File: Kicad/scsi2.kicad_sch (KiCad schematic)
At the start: 30 parts, among them J3 TO-LED, J4 TO-MB, J8 TO-A3000-LED, J9 TO-A3000-MB, U10 NCR53c710 SCSI Host Controller, U13 SST39SF010/020/040, Y1 Abracon ACO-50MHz

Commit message: Add more LCSC parts and mark some parts DNP
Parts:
- C1001, C1003, C1005, C1007, C1009: LCSC Part # (none) -> C14663
- FB1, FB2, FB3, R11: LCSC Part # (none) -> C95177
- J3, J4, J8, J9: LCSC Part # (none) -> C6332196
- R13: LCSC Part # (none) -> C22548
- R9: LCSC Part # (none) -> C114640
- RN10, RN17, RN6, RN7, RN8: LCSC Part # (none) -> C784824
- U13: LCSC Part # (none) -> C72450
- Y1: LCSC Part # (none) -> C7431196

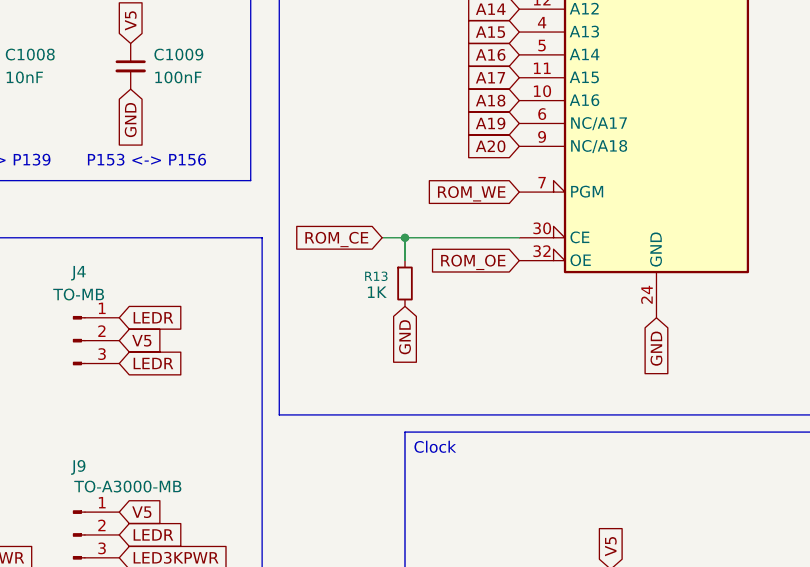
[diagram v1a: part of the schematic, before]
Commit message: Add remaining part numbers, remove C20, C30, C31
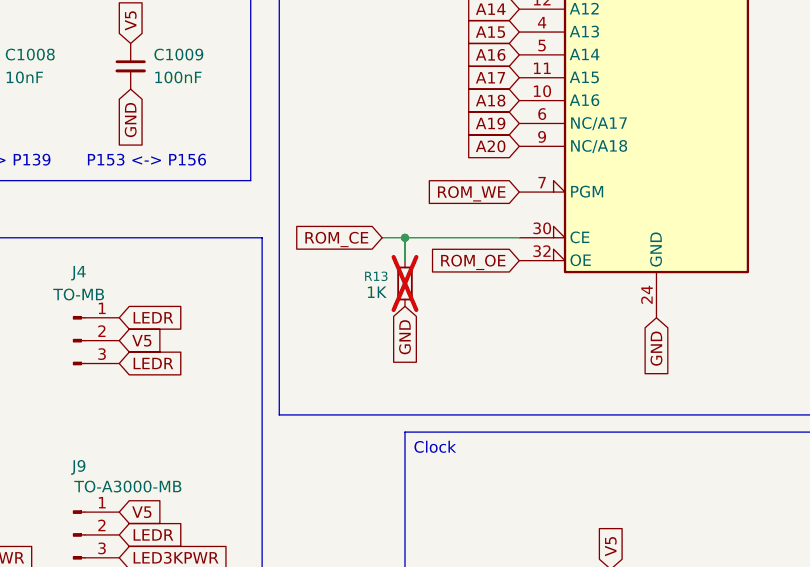
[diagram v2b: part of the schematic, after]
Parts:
- C1002, C1004, C1006, C1008, C32: LCSC Part # (none) -> C100042
- D2: LCSC Part # (none) -> C965821
- R10: LCSC Part # (none) -> C114662
- R13: now not fitted
- U10: LCSC Part # (none) -> C9900133089
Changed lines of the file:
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@@
 			)
 		)
-		(property "LCSC Part #" ""
+		(property "LCSC Part #" "C100042"
 			(at 234.95 129.54 0)
 			(effects
@@
 			)
 		)
-		(property "LCSC Part #" ""
+		(property "LCSC Part #" "C100042"
 			(at 165.1 46.99 0)
 			(effects
@@
 			)
 		)
-		(property "LCSC Part #" ""
+		(property "LCSC Part #" "C965821"
 			(at 186.69 146.05 0)
 			(effects
@@
 			)
 		)
-		(property "LCSC Part #" ""
+		(property "LCSC Part #" "C100042"
 			(at 182.88 67.31 0)
 			(effects
@@
 			)
 		)
-		(property "LCSC Part #" ""
+		(property "LCSC Part #" "C100042"
 			(at 199.39 46.99 0)
 			(effects
@@
 		(in_bom yes)
 		(on_board yes)
-		(dnp no)
+		(dnp yes)
 		(property "Reference" "R13"
 			(at 225.298 90.678 0)
@@
 			)
 		)
-		(property "LCSC Part #" ""
+		(property "LCSC Part #" "C9900133089"
 			(at 133.35 55.88 0)
 			(effects
@@
 			)
 		)
-		(property "LCSC Part #" ""
+		(property "LCSC Part #" "C114662"
 			(at 191.77 146.05 90)
 			(effects
@@
 			)
 		)
-		(property "LCSC Part #" ""
+		(property "LCSC Part #" "C100042"
 			(at 182.88 26.67 0)
 			(effects
@@
 			)
 		)
-		(property "LCSC Part #" ""
+		(property "LCSC Part #" "C9900133089"
 			(at 58.42 58.42 0)
 			(effects

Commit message: Fix LCSC parts issues
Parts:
- U13: LCSC Part # C72450 -> C630569
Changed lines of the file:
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@@
 			)
 		)
-		(property "LCSC Part #" "C72450"
+		(property "LCSC Part #" "C630569"
 			(at 257.81 60.96 0)
 			(effects

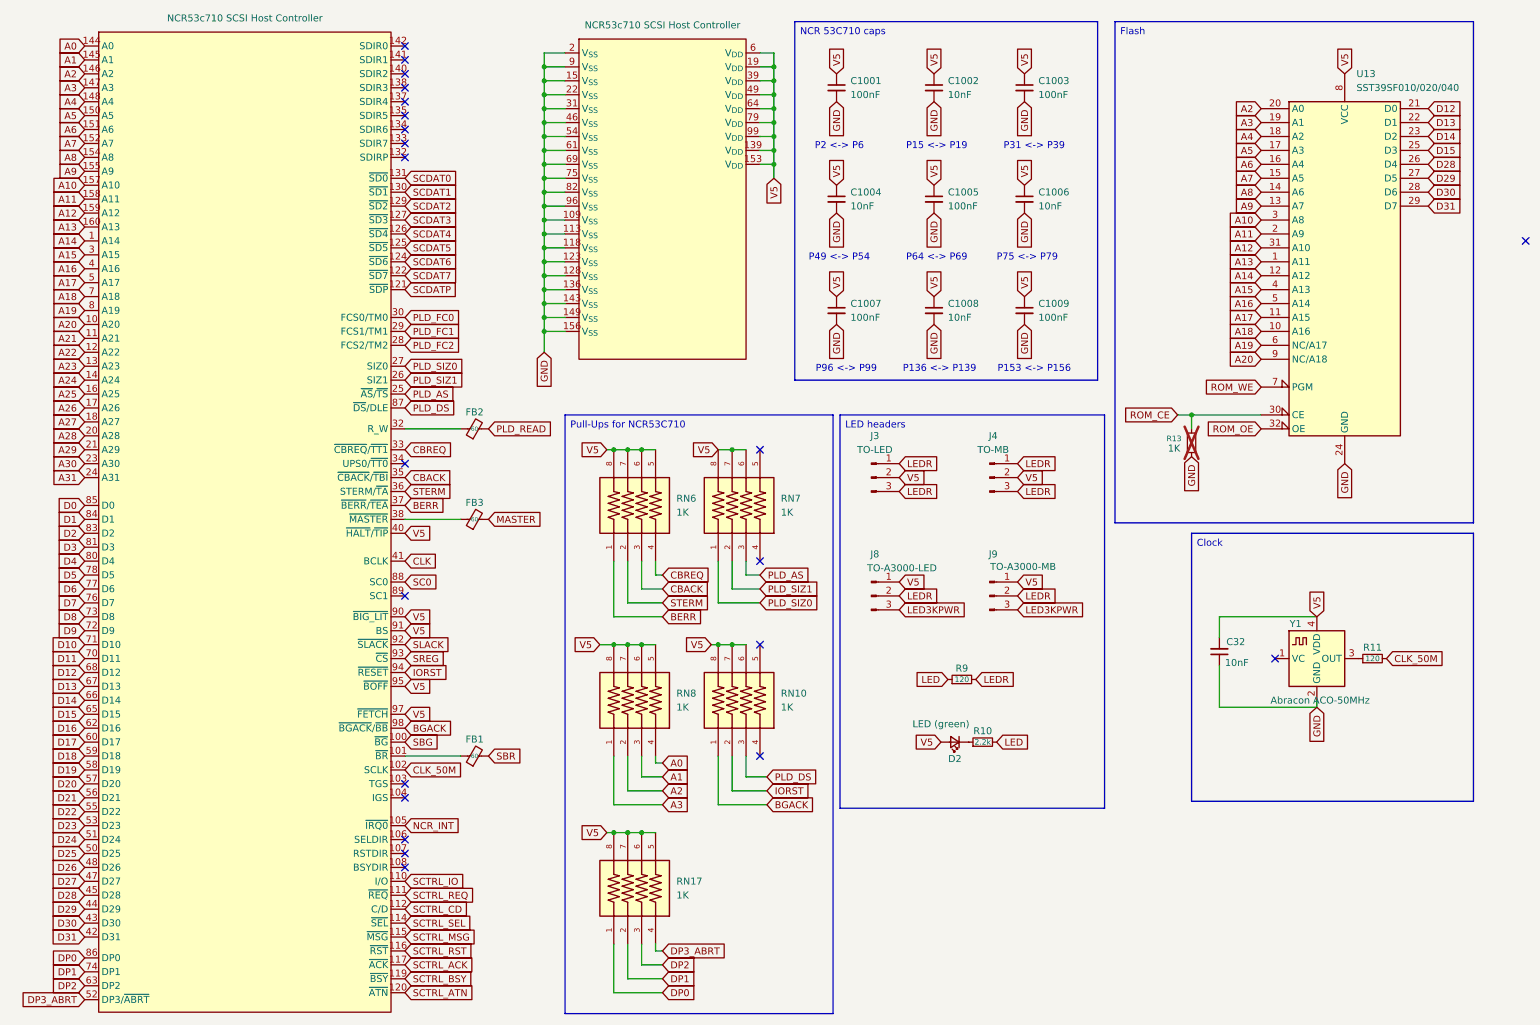
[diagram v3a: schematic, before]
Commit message: Add fiducials and clean up schematics
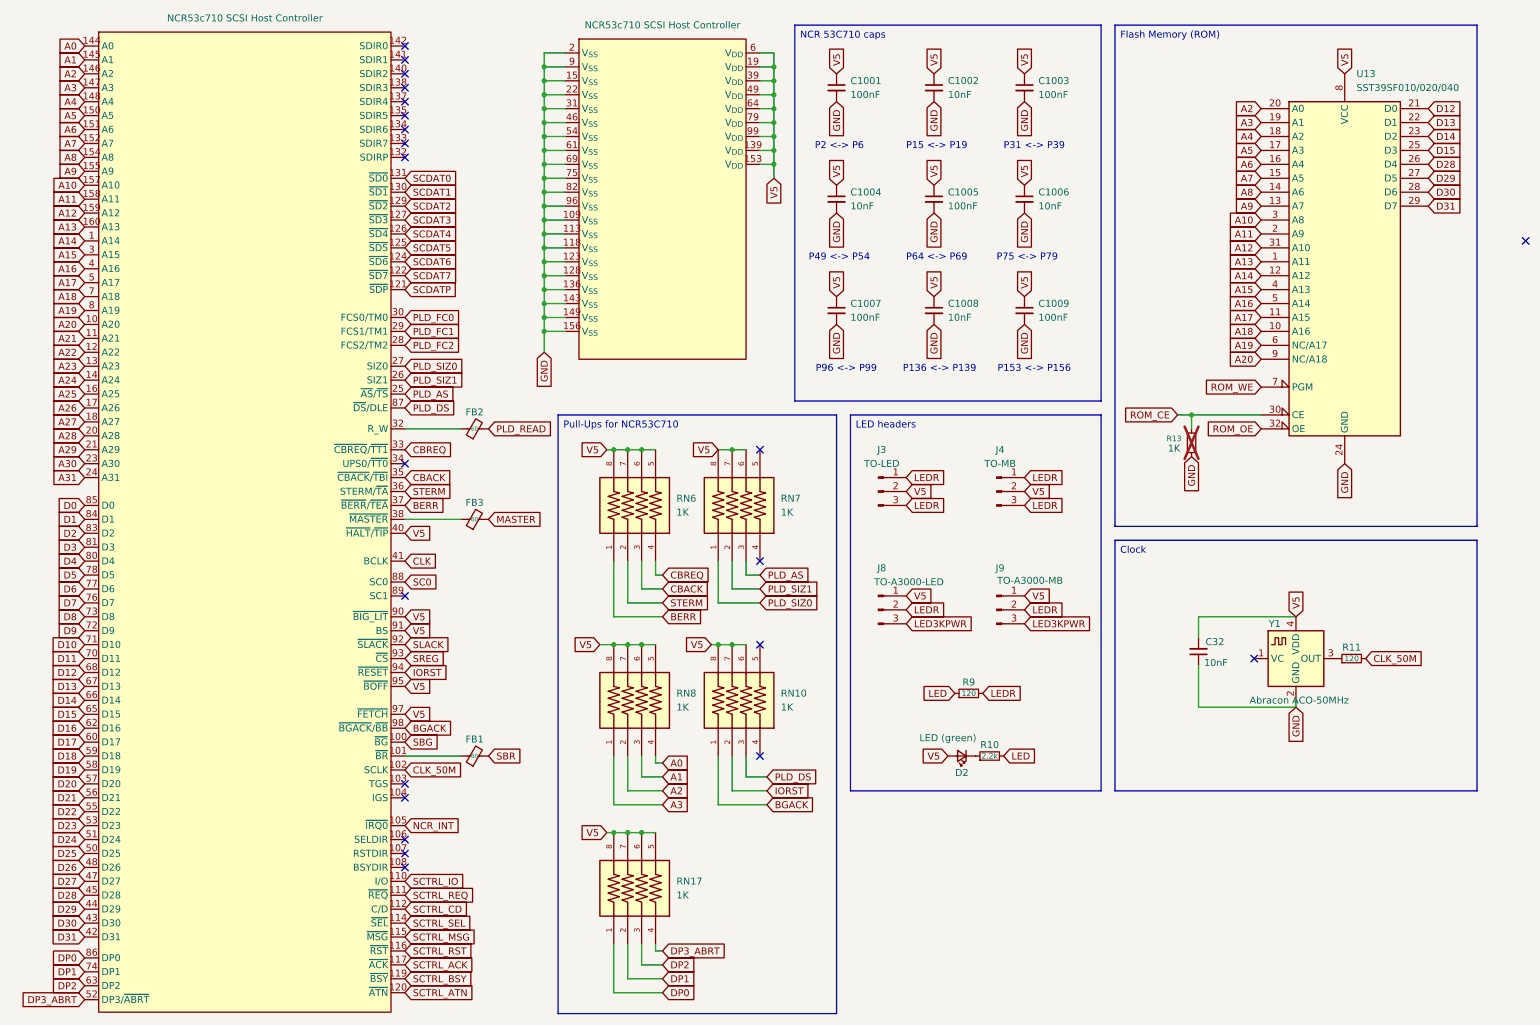
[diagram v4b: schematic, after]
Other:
- moved on the sheet: C32, D2, J3, J4, J8, J9, R10, R11, R9, Y1

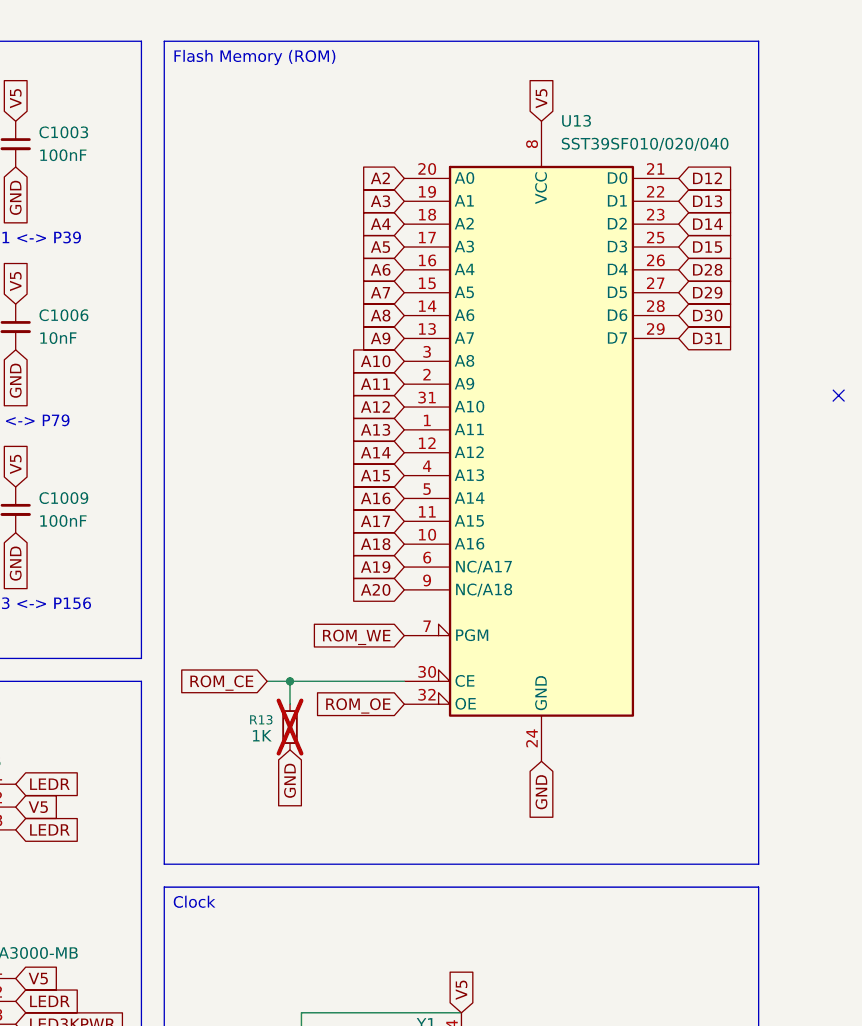
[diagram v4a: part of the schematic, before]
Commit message: Add SPI flash option and move flash to its own page
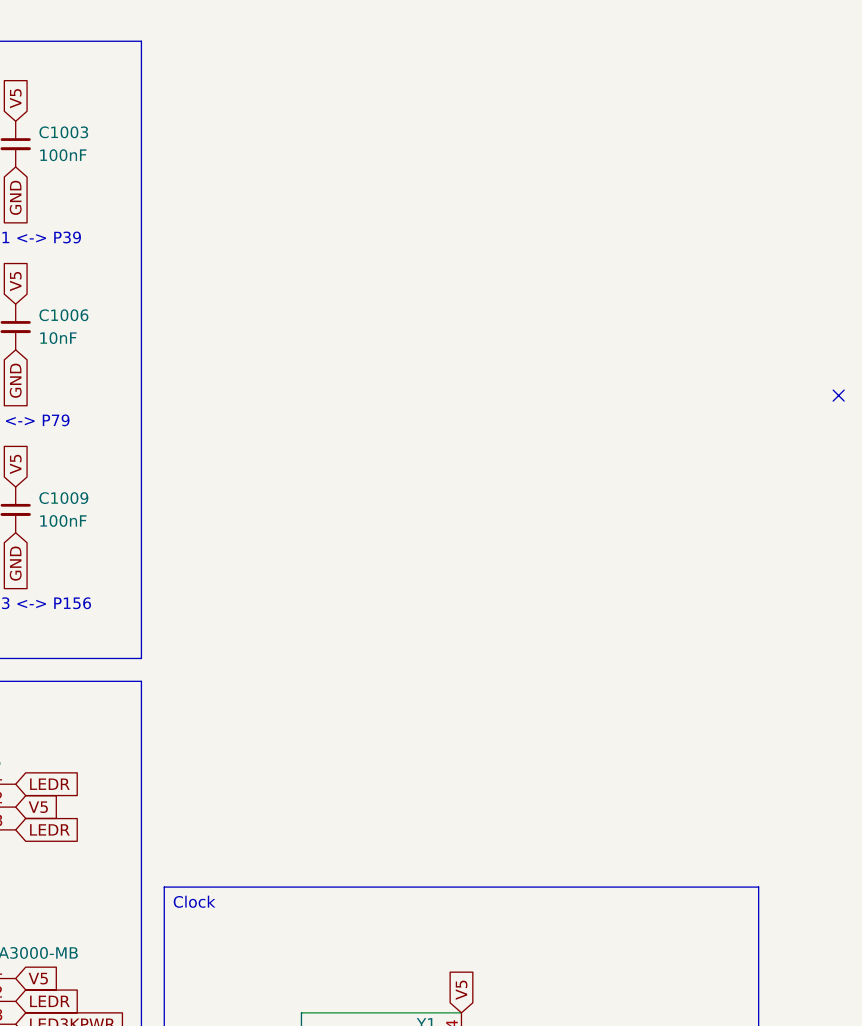
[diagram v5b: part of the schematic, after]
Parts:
- removed R13: 1K, Resistor_SMD:R_0603_1608Metric, symbol Device:R_Small
- removed U13: SST39SF010/020/040, Package_SO:TSSOP-32_8x11mm_P0.65mm, symbol 39SF010-TSOP:SST39SF010

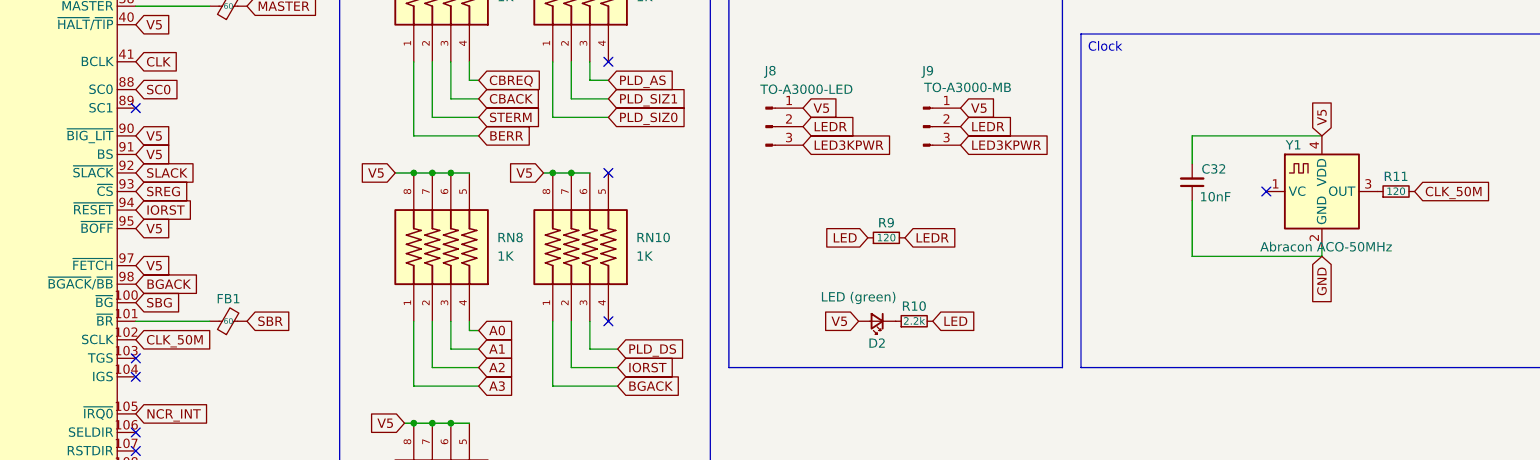
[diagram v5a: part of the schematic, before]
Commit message: Review fixes on scsi2 page
* R11 is 22 Ohm not 120 in the original schematics
* FETCH# is NC in the original, not V5
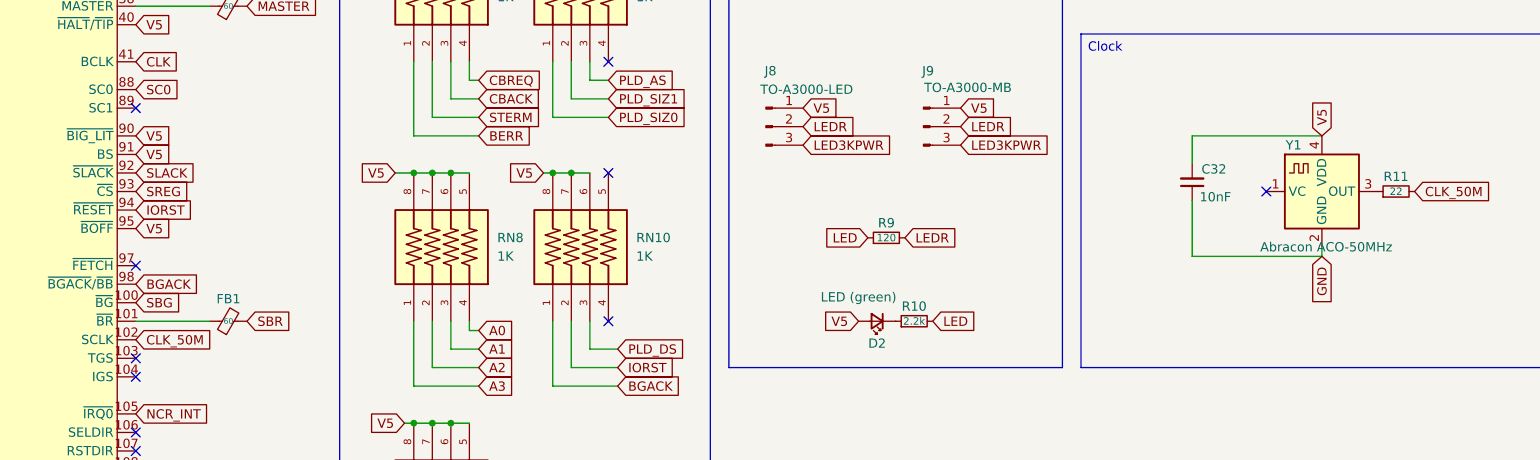
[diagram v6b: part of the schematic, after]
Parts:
- R11: value 120 -> 22
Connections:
- net V5: no longer U10.97 (~{FETCH})
- no-connect marks 22 -> 23
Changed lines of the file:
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@@
 	)
 	(no_connect
+		(at 86.36 140.97)
+	)
+	(no_connect
 		(at 86.36 34.29)
 	)
@@
 		)
 	)
-	(global_label "V5"
-		(shape input)
-		(at 86.36 140.97 0)
-		(fields_autoplaced yes)
-		(effects
-			(font
-				(size 1.27 1.27)
-			)
-			(justify left)
-		)
-		(property "Intersheetrefs" "${INTERSHEET_REFS}"
-			(at 91.6433 140.97 0)
-			(effects
-				(font
-					(size 1.27 1.27)
-				)
-				(justify left)
-				(hide yes)
-			)
-		)
-	)
 	(global_label "SCTRL_BSY"
 		(shape input)
@@
 			)
 		)
-		(property "Value" "120"
+		(property "Value" "22"
 			(at 259.08 130.81 90)
 			(effects
